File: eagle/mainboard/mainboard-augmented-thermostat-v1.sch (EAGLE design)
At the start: 12 parts, among them Q1 RS485-ADAPTER0.05-CONNECTOR, X1 RJ45-6L21-B

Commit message: Added fourth DMP180 sensor, right on the mainboard, so that we can compare to ambient pressure, if we need to.
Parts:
- added BMP180: (no value), con-amp-quick:M04
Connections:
- new net 1Y3: BMP180.4, U$2.1Y3
- new net 2Y3: BMP180.3, U$2.2Y3
- net +3V3: now also BMP180.1
- net GND: now also BMP180.2
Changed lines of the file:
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@@
 <part name="P+1" library="supply1" deviceset="+12V" device=""/>
 <part name="P+5" library="supply1" deviceset="+5V" device=""/>
+<part name="BMP180" library="con-amp-quick" deviceset="M04" device=""/>
+<part name="GND6" library="supply1" deviceset="GND" device=""/>
+<part name="+3V9" library="supply1" deviceset="+3V3" device=""/>
 </parts>
 <sheets>
@@
 <instance part="P+1" gate="1" x="264.16" y="99.06" rot="R270"/>
 <instance part="P+5" gate="1" x="228.6" y="99.06" rot="R90"/>
+<instance part="BMP180" gate="G$1" x="195.58" y="38.1" rot="R180"/>
+<instance part="GND6" gate="1" x="177.8" y="22.86"/>
+<instance part="+3V9" gate="G$1" x="185.42" y="48.26"/>
 </instances>
 <busses>
@@
 <wire x1="259.08" y1="88.9" x2="259.08" y2="81.28" width="0.1524" layer="91"/>
 </segment>
+<segment>
+<pinref part="BMP180" gate="G$1" pin="2"/>
+<pinref part="GND6" gate="1" pin="GND"/>
+<wire x1="190.5" y1="38.1" x2="177.8" y2="38.1" width="0.1524" layer="91"/>
+<wire x1="177.8" y1="38.1" x2="177.8" y2="25.4" width="0.1524" layer="91"/>
+</segment>
 </net>
 <net name="+12V" class="0">
@@
 <wire x1="200.66" y1="147.32" x2="200.66" y2="149.86" width="0.1524" layer="91"/>
 </segment>
-</net>
+<segment>
+<pinref part="BMP180" gate="G$1" pin="1"/>
+<wire x1="190.5" y1="40.64" x2="185.42" y2="40.64" width="0.1524" layer="91"/>
+<wire x1="185.42" y1="40.64" x2="185.42" y2="45.72" width="0.1524" layer="91"/>
+<pinref part="+3V9" gate="G$1" pin="+3V3"/>
+</segment>
+</net>
+<net name="2Y3" class="0">
+<segment>
+<pinref part="BMP180" gate="G$1" pin="3"/>
+<wire x1="190.5" y1="35.56" x2="185.42" y2="35.56" width="0.1524" layer="91"/>
+<label x="182.88" y="35.56" size="1.778" layer="95"/>
+</segment>
+<segment>
+<pinref part="U$2" gate="G$1" pin="2Y3"/>
+<wire x1="146.05" y1="16.51" x2="148.59" y2="16.51" width="0.1524" layer="91"/>
+<label x="148.59" y="16.51" size="1.778" layer="95"/>
+</segment>
+</net>
+<net name="1Y3" class="0">
+<segment>
+<pinref part="BMP180" gate="G$1" pin="4"/>
+<wire x1="190.5" y1="33.02" x2="185.42" y2="33.02" width="0.1524" layer="91"/>
+<label x="182.88" y="33.02" size="1.778" layer="95"/>
+</segment>
+<segment>
+<pinref part="U$2" gate="G$1" pin="1Y3"/>
+<wire x1="146.05" y1="34.29" x2="148.844" y2="34.29" width="0.1524" layer="91"/>
+<label x="148.844" y="34.29" size="1.778" layer="95"/>
+</segment>
+</net>

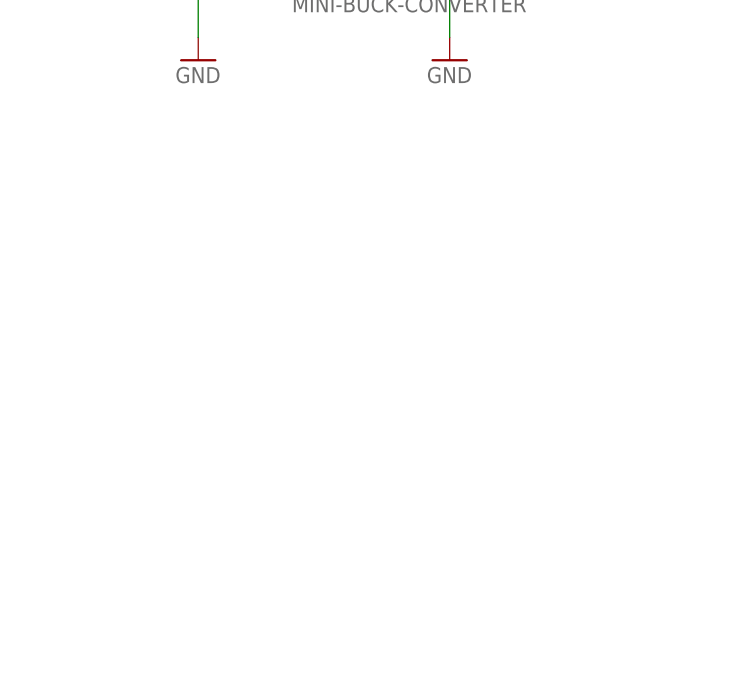
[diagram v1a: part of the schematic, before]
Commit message: Added buzzer to the mainboard. Ready for first prototype!
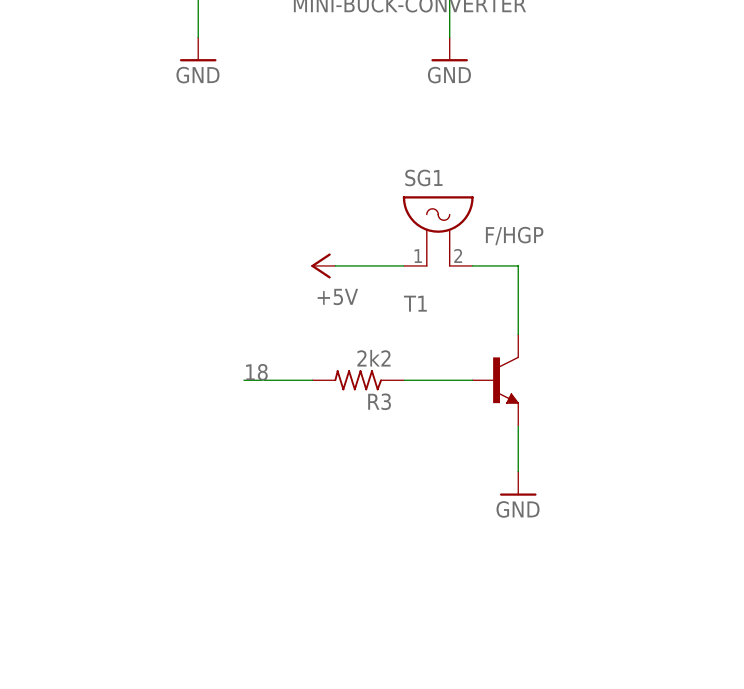
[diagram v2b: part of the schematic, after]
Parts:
- added R3: 2k2, adafruit:R-US_R0603
- added SG1: F/HGP, buzzer:F/HGP
- added T1: (no value), transistor:BC808-NPN-SOT23-BEC
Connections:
- new net N$1: R3.1, T1.B
- new net N$2: SG1.2, T1.C
- net +5V: now also SG1.1
- net 18: now also R3.2
- net GND: now also T1.E
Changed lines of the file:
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@@
 <part name="GND6" library="supply1" deviceset="GND" device=""/>
 <part name="+3V9" library="supply1" deviceset="+3V3" device=""/>
+<part name="SG1" library="buzzer" deviceset="F/HGP" device=""/>
+<part name="T1" library="transistor" deviceset="*-NPN-" device="SOT23-BEC" technology="BC808"/>
+<part name="R3" library="adafruit" deviceset="R-US_" device="R0603" value="2k2"/>
+<part name="GND8" library="supply1" deviceset="GND" device=""/>
+<part name="P+6" library="supply1" deviceset="+5V" device=""/>
 </parts>
 <sheets>
@@
 <instance part="GND6" gate="1" x="177.8" y="22.86"/>
 <instance part="+3V9" gate="G$1" x="185.42" y="48.26"/>
+<instance part="SG1" gate="G$1" x="256.54" y="58.42"/>
+<instance part="T1" gate="G$1" x="264.16" y="43.18"/>
+<instance part="R3" gate="G$1" x="248.92" y="43.18" rot="R180"/>
+<instance part="GND8" gate="1" x="266.7" y="30.48"/>
+<instance part="P+6" gate="1" x="243.84" y="55.88" rot="R90"/>
 </instances>
 <busses>
@@
 <wire x1="177.8" y1="38.1" x2="177.8" y2="25.4" width="0.1524" layer="91"/>
 </segment>
+<segment>
+<pinref part="GND8" gate="1" pin="GND"/>
+<pinref part="T1" gate="G$1" pin="E"/>
+<wire x1="266.7" y1="33.02" x2="266.7" y2="38.1" width="0.1524" layer="91"/>
+</segment>
 </net>
 <net name="+12V" class="0">
@@
 <label x="203.2" y="101.6" size="1.778" layer="95"/>
 </segment>
+<segment>
+<pinref part="R3" gate="G$1" pin="2"/>
+<wire x1="243.84" y1="43.18" x2="236.22" y2="43.18" width="0.1524" layer="91"/>
+<label x="236.22" y="43.18" size="1.778" layer="95"/>
+</segment>
 </net>
 <net name="17" class="0">
@@
 <wire x1="236.22" y1="99.06" x2="231.14" y2="99.06" width="0.1524" layer="91"/>
 <pinref part="P+5" gate="1" pin="+5V"/>
+</segment>
+<segment>
+<pinref part="SG1" gate="G$1" pin="1"/>
+<pinref part="P+6" gate="1" pin="+5V"/>
+<wire x1="254" y1="55.88" x2="246.38" y2="55.88" width="0.1524" layer="91"/>
 </segment>
 </net>
@@
 </segment>
 </net>
+<net name="N$1" class="0">
+<segment>
+<pinref part="R3" gate="G$1" pin="1"/>
+<pinref part="T1" gate="G$1" pin="B"/>
+<wire x1="254" y1="43.18" x2="261.62" y2="43.18" width="0.1524" layer="91"/>
+</segment>
+</net>
+<net name="N$2" class="0">
+<segment>
+<pinref part="SG1" gate="G$1" pin="2"/>
+<pinref part="T1" gate="G$1" pin="C"/>
+<wire x1="261.62" y1="55.88" x2="266.7" y2="55.88" width="0.1524" layer="91"/>
+<wire x1="266.7" y1="55.88" x2="266.7" y2="48.26" width="0.1524" layer="91"/>
+</segment>
+</net>
